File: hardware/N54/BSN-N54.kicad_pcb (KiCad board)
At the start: 4 copper layers, 34 x 34 mm, 44 parts, among them J1 Conn_Coaxial_Small, U1 nRF54L05-QFXX, U2 SHTC3, U3 HDC2010, X1 32MHz, X2 32.768kHz

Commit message: Cleaned up libraries for both variants
Renamed the project libraries to BSN-N54 / BSN-C23 and updated lib tables and all references, removed Nordic parts and the unused 40-pin CC2340 package from the C23 library, synced Antenna symbol fields to N54, updated READMEs.
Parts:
- AE1: footprint BLE_Sensor_Node:AANI-CH-0138-Q-T -> BSN-N54:AANI-CH-0138-Q-T
- U1: footprint BLE_Sensor_Node:VQFN-48-1EP_6x6mm_P0.4mm_EP4.1x4.1mm_ThermalVias -> BSN-N54:VQFN-48-1EP_6x6mm_P0.4mm_EP4.1x4.1mm_ThermalVias
- U3: footprint BLE_Sensor_Node:HDC2010 -> BSN-N54:HDC2010
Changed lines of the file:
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@@
 		)
 	)
-	(footprint "BLE_Sensor_Node:HDC2010"
+	(footprint "BSN-N54:HDC2010"
 		(layer "F.Cu")
 		(at 159.2 106 90)
@@
 		)
 	)
-	(footprint "BLE_Sensor_Node:VQFN-48-1EP_6x6mm_P0.4mm_EP4.1x4.1mm_ThermalVias"
+	(footprint "BSN-N54:VQFN-48-1EP_6x6mm_P0.4mm_EP4.1x4.1mm_ThermalVias"
 		(locked yes)
 		(layer "F.Cu")
@@
 		)
 		(embedded_fonts no)
-		(model "${KIPRJMOD}/library/3d_models/QFN-48-1EP_6x6_P04mm.STEP"
+		(model "${KIPRJMOD}/library/3d_models/VQFN-48-1EP_6x6mm_P0.4mm_EP4.1x4.1mm.step"
 			(offset
 				(xyz 0 0 0)
@@
 		)
 	)
-	(footprint "BLE_Sensor_Node:AANI-CH-0138-Q-T"
+	(footprint "BSN-N54:AANI-CH-0138-Q-T"
 		(layer "F.Cu")
 		(at 150 84.75)

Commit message: Slikscreen cleanup
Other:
- board text added: "INT"
- board text added: "SCL"
- board text added: "SDA"
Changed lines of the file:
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@@
 		)
 	)
-	(gr_text "RST"
+	(gr_text "SDA"
 		(at 160.1 103.4 0)
 		(layer "F.SilkS")
@@
 		)
 	)
-	(gr_text "RST"
+	(gr_text "SCL"
 		(at 160.8 100.8 0)
 		(layer "F.SilkS")
@@
 		)
 	)
-	(gr_text "RST"
+	(gr_text "INT"
 		(at 164.5 105.5 0)
 		(layer "F.SilkS")

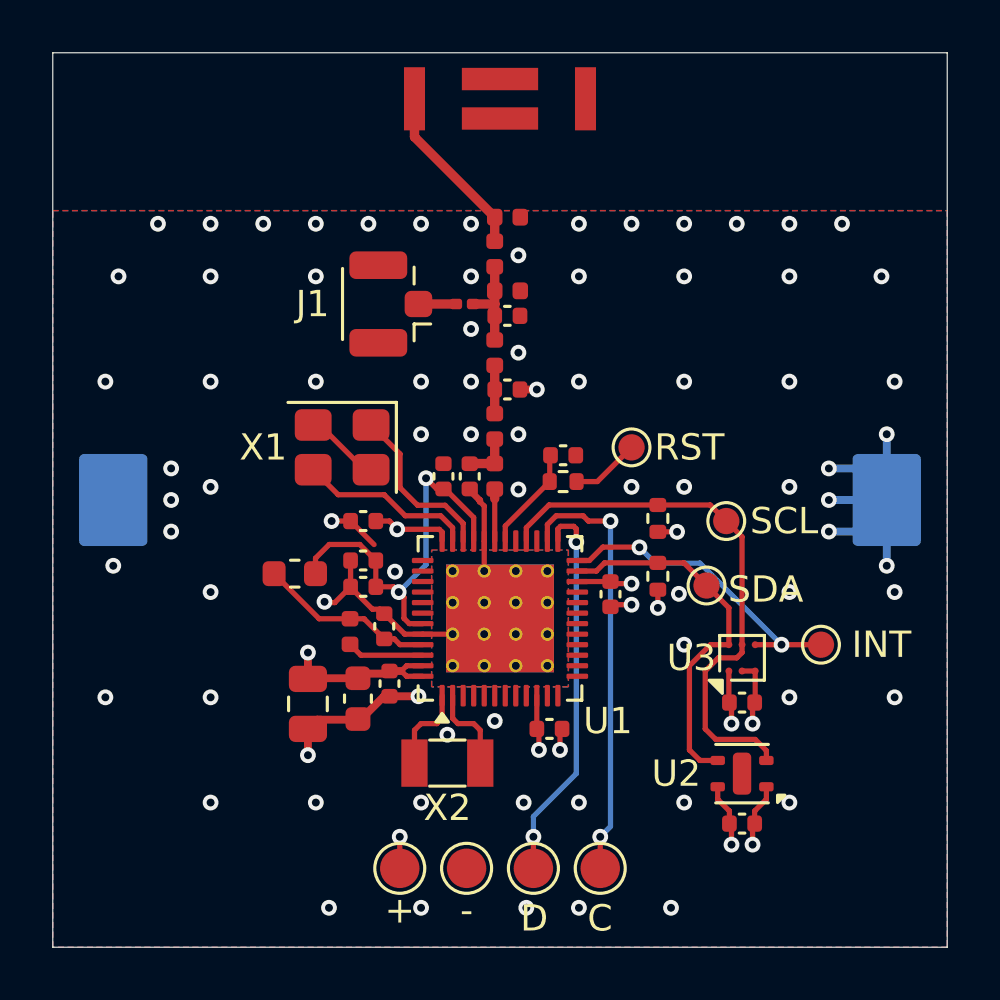
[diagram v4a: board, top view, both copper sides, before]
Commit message: Matched components & Footrpints. Small routing changes on N54
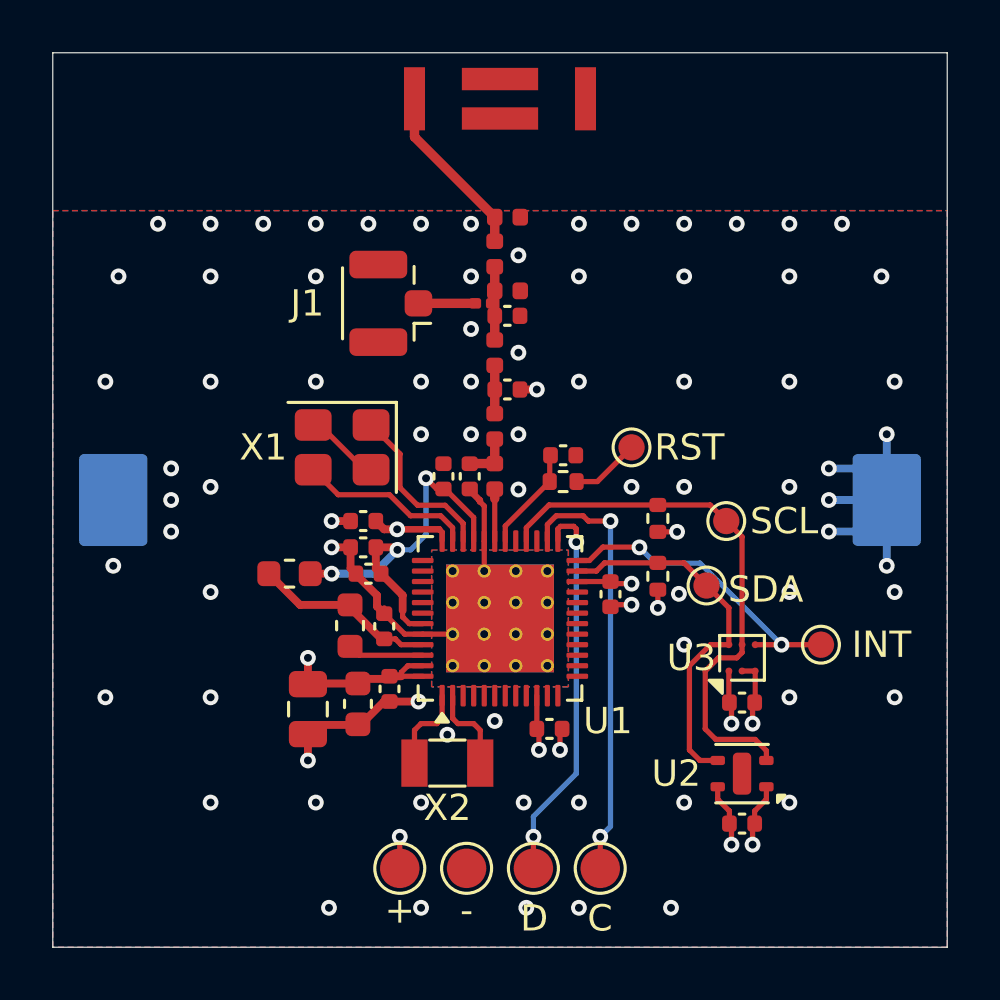
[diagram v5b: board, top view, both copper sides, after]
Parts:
- L1: footprint Inductor_SMD:L_0402_1005Metric -> Inductor_SMD:L_0603_1608Metric
- moved R4 0.73 mm to (149.4, 92.5)
- moved C7 0.54 mm to (145.0, 102.8)
- moved C8 0.50 mm to (144.8, 101.8)
- moved L1 0.22 mm to (144.3, 104.8)
- moved C1 0.20 mm to (144.6, 107.8)
- moved C10 0.20 mm to (142.7, 107.9)
- moved C2 0.20 mm to (145.8, 107.2)
- moved FB1 0.20 mm to (142.0, 102.8)
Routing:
- net GND: track 28.1 -> 26.9 mm, vias 78 -> 77
- net Net-(C16-Pad1): track 3.61 -> 2.78 mm
- net Net-(J1-In): track 1.43 -> 2.16 mm
- net Net-(U1-DECA): vias 2 -> 3

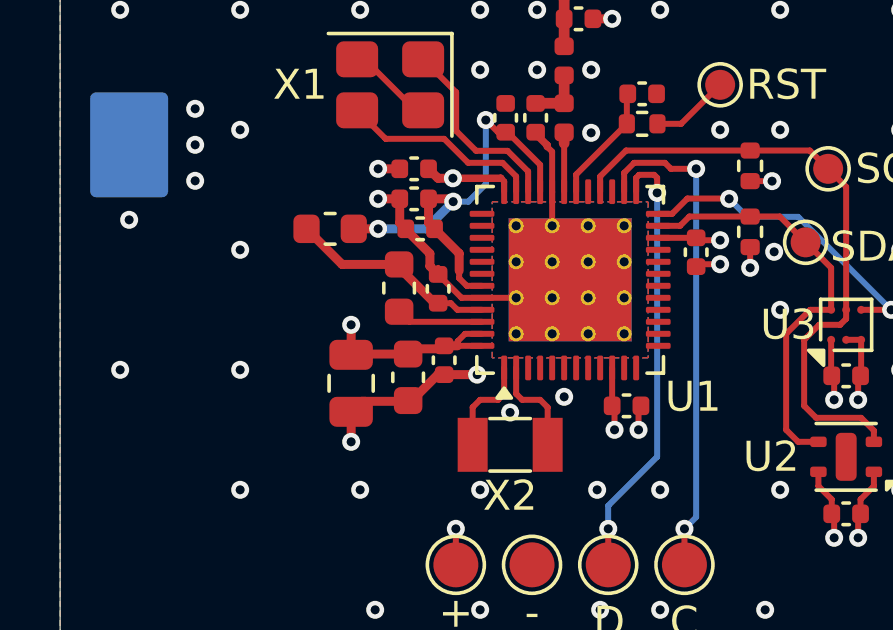
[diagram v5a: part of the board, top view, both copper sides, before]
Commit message: Progress on C23 layout & Routing
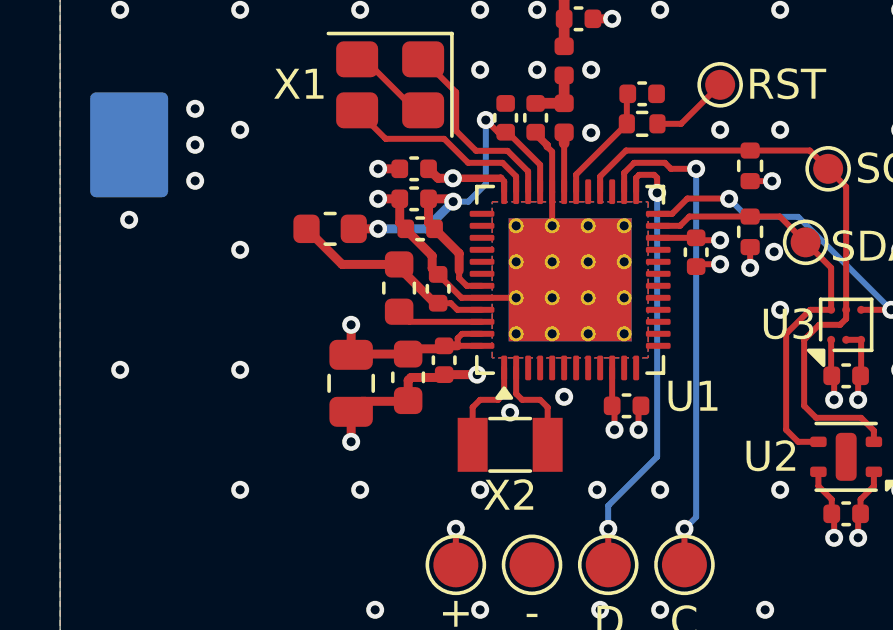
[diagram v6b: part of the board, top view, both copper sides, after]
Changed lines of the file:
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@@
-	)
-	(segment
-		(start 146.5 106.3)
-		(end 146.25 106.55)
-		(width 0.2)
-		(layer "F.Cu")
-		(net "VDD")
 	)
 	(segment
@@
 	)
 	(segment
+		(start 147.0625 106.3)
+		(end 146.4 106.3)
+		(width 0.2)
+		(layer "F.Cu")
+		(net "VDD")
+	)
+	(segment
 		(start 145.7 106.8)
 		(end 145.8 106.7)
@@
 	)
 	(segment
-		(start 147.0625 106.3)
-		(end 146.5 106.3)
-		(width 0.2)
-		(layer "F.Cu")
-		(net "VDD")
-	)
-	(segment
 		(start 144.6 106.975)
 		(end 144.775 106.8)
@@
 		(end 146.091302 101.114496)
 		(width 0.3)
+		(layer "F.Cu")
+		(net "VDD")
+	)
+	(segment
+		(start 146.25 106.45)
+		(end 146.25 106.7)
+		(width 0.2)
 		(layer "F.Cu")
 		(net "VDD")
@@
 	)
 	(segment
+		(start 146.4 106.3)
+		(end 146.25 106.45)
+		(width 0.2)
+		(layer "F.Cu")
+		(net "VDD")
+	)
+	(segment
 		(start 154.2 103.1)
 		(end 152.9375 103.1)
@@
 	)
 	(segment
-		(start 146.25 106.55)
-		(end 146.25 106.7)
-		(width 0.2)
-		(layer "F.Cu")
-		(net "VDD")
-	)
-	(segment
 		(start 142.725 106.975)
 		(end 142.7 107)
@@
 	)
 	(segment
+		(start 145.705 107.755)
+		(end 144.695 107.755)
+		(width 0.3)
+		(layer "F.Cu")
+		(net "GND")
+	)
+	(segment
 		(start 144.32 101.8)
 		(end 144.32 102.6)
@@
 	)
 	(segment
+		(start 144.52 102.82)
+		(end 145.4 103.7)
+		(width 0.3)
+		(layer "F.Cu")
+		(net "GND")
+	)
+	(segment
 		(start 159.2 106.499997)
 		(end 159.200002 106.499999)
@@
 		(start 144.575 108.55)
 		(end 143.049998 108.55)
+		(width 0.3)
+		(layer "F.Cu")
+		(net "GND")
+	)
+	(segment
+		(start 144.52 102.8)
+		(end 144.52 102.82)
 		(width 0.3)
 		(layer "F.Cu")
@@
 	)
 	(segment
-		(start 145.59 107.66)
-		(end 144.725 108.525)
-		(width 0.3)
-		(layer "F.Cu")
-		(net "GND")
-	)
-	(segment
 		(start 159.7 107.679999)
 		(end 159.68 107.699999)
@@
 	)
 	(segment
-		(start 144.725 108.525)
-		(end 144.6 108.525)
-		(width 0.3)
-		(layer "F.Cu")
-		(net "GND")
-	)
-	(segment
 		(start 159.7 106.5)
 		(end 159.7 107.679999)
@@
 	(segment
 		(start 145.8 107.66)
-		(end 145.59 107.66)
+		(end 145.705 107.755)
 		(width 0.3)
 		(layer "F.Cu")
@@
 	)
 	(segment
-		(start 145.324926 104.044926)
-		(end 145.6 104.32)
-		(width 0.3)
-		(layer "F.Cu")
-		(net "GND")
-	)
-	(segment
-		(start 145.6 104.32)
-		(end 145.6 104.1)
-		(width 0.2)
-		(layer "F.Cu")
-		(net "GND")
-	)
-	(segment
 		(start 154.280001 103.98)
 		(end 154.200001 104.06)
@@
 	)
 	(segment
-		(start 144.52 102.8)
-		(end 144.52 102.82)
+		(start 144.695 107.755)
+		(end 144.6 107.85)
 		(width 0.3)
 		(layer "F.Cu")
@@
 		(end 152.36 108.7)
 		(width 0.2)
+		(layer "F.Cu")
+		(net "GND")
+	)
+	(segment
+		(start 145.4 104.12)
+		(end 145.6 104.32)
+		(width 0.3)
 		(layer "F.Cu")
 		(net "GND")
@@
 	)
 	(segment
-		(start 145.324926 103.624926)
-		(end 145.324926 104.044926)
-		(width 0.3)
-		(layer "F.Cu")
-		(net "GND")
-	)
-	(segment
 		(start 144.32 102.6)
 		(end 144.52 102.8)
@@
 	)
 	(segment
-		(start 144.52 102.82)
-		(end 145.324926 103.624926)
-		(width 0.3)
-		(layer "F.Cu")
-		(net "GND")
-	)
-	(segment
 		(start 149.4 101.5625)
 		(end 149.4 102.7)
@@
 	)
 	(segment
+		(start 145.4 103.7)
+		(end 145.4 104.12)
+		(width 0.3)
+		(layer "F.Cu")
+		(net "GND")
+	)
+	(segment
 		(start 144.85 98.85)
 		(end 143.15 97.15)
@@
 		(end 159.6 107.78)
 		(width 0.2)
+		(layer "F.Cu")
+		(net "GND")
+	)
+	(segment
+		(start 144.6 107.85)
+		(end 144.6 108.525)
+		(width 0.3)
 		(layer "F.Cu")
 		(net "GND")
@@
 			)
 		)
+	)
+	(zone
+		(layer "F.Cu")
+		(hatch edge 0.5)
+		(connect_pads
+			(clearance 0)
+		)
+		(min_thickness 0.15)
+		(keepout
+			(tracks allowed)
+			(vias allowed)
+			(pads allowed)
+			(copperpour not_allowed)
+			(footprints allowed)
+		)
+		(placement
+			(enabled no)
+			(sheetname "/")
+		)
+		(fill
+			(thermal_gap 0.5)
+			(thermal_bridge_width 0.3)
+			(island_removal_mode 0)
+		)
+		(polygon
+			(pts
+				(xy 143.25 97.4) (xy 144.75 97.4) (xy 144.75 98.2) (xy 144.25 98.7) (xy 143.75 98.7) (xy 143.25 98.2)
+			)
+		)
+	)
+	(zone
+		(layer "F.Cu")
+		(hatch edge 0.5)
+		(connect_pads
+			(clearance 0)
+		)
+		(min_thickness 0.15)
+		(keepout
+			(tracks allowed)
+			(vias allowed)
+			(pads allowed)
+			(copperpour not_allowed)
+			(footprints allowed)
+		)
+		(placement
+			(enabled no)
+			(sheetname "/")
+		)
+		(fill
+			(thermal_gap 0.5)
+			(thermal_bridge_width 0.3)
+			(island_removal_mode 0)
+		)
+		(polygon
+			(pts
+				(xy 144.65 103.15) (xy 146.15 103.15) (xy 146.15 103.95) (xy 145.65 104.45) (xy 145.15 104.45) (xy 144.65 103.95)
+			)
+		)
+	)
+	(zone
+		(layer "F.Cu")
+		(hatch edge 0.5)
+		(connect_pads
+			(clearance 0)
+		)
+		(min_thickness 0.15)
+		(keepout
+			(tracks allowed)
+			(vias allowed)
+			(pads allowed)
+			(copperpour not_allowed)
+			(footprints allowed)
+		)
+		(placement
+			(enabled no)
+			(sheetname "/")
+		)
+		(fill
+			(thermal_gap 0.5)
+			(thermal_bridge_width 0.3)
+			(island_removal_mode 0)
+		)
+		(polygon
+			(pts
+				(xy 142.85 106.75) (xy 144.386434 106.75) (xy 144.386434 107.55) (xy 143.886434 108.05) (xy 142.85 108.05)
+			)
+		)

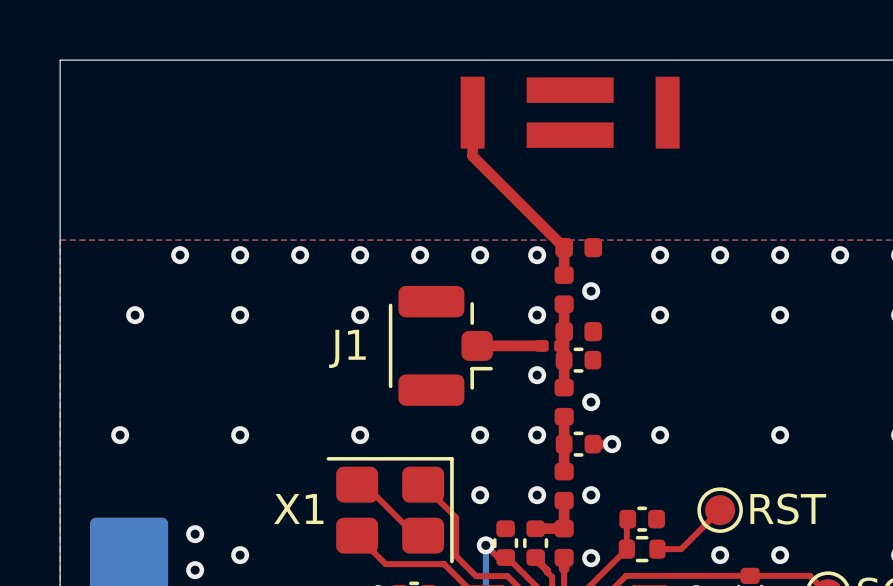
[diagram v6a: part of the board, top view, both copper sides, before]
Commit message: Moved the U.FL connector closer to the matching network
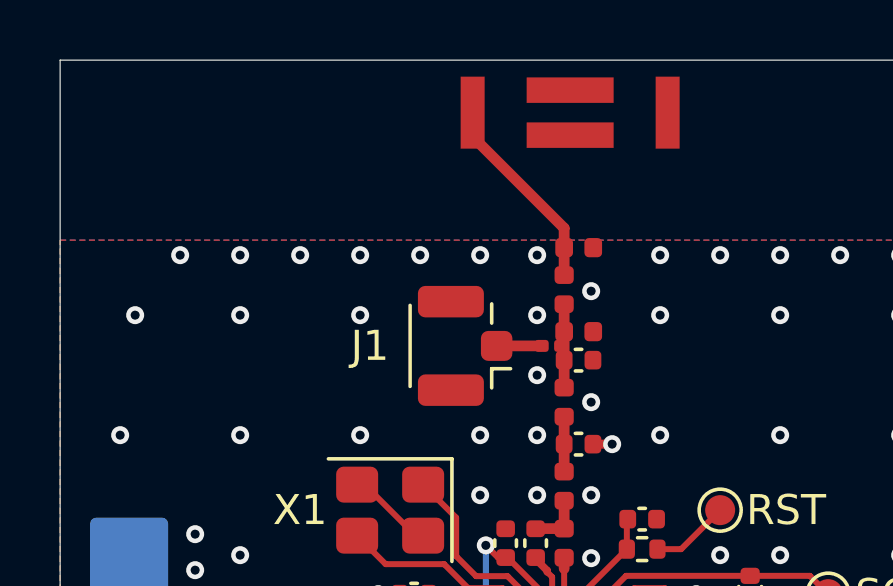
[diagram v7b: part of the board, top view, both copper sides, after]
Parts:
- moved J1 0.65 mm to (146.0, 92.5)
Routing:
- net Net-(J1-In): track 2.16 -> 1.50 mm
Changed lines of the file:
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@@
 	(footprint "Connector_Coaxial:U.FL_Hirose_U.FL-R-SMT-1_Vertical"
 		(layer "F.Cu")
-		(at 145.375 92.525 180)
+		(at 146.025 92.525 180)
 		(descr "Hirose U.FL Coaxial (https://www.hirose.com/en/product/document?clcode=CL0331-0472-2-01&productname=U.FL-R-SMT-1(01)&series=U.FL&documenttype=2DDrawing&lang=en&documentid=0000940668)")
 		(tags "Hirose U.FL Coaxial")
@@
 			(polygon
 				(pts
-					(xy 144.275 93.475) (xy 146.365 93.475) (xy 146.365 91.575) (xy 144.275 91.575)
+					(xy 144.925 93.475) (xy 147.015 93.475) (xy 147.015 91.575) (xy 144.925 91.575)
 				)
 			)
@@
 	)
 	(segment
-		(start 149.8 89.25)
-		(end 146.75 86.2)
+		(start 149.8 90.165)
+		(end 149.8 89.25)
 		(width 0.3586)
 		(layer "F.Cu")
@@
 	)
 	(segment
-		(start 149.8 90.165)
-		(end 149.8 89.25)
+		(start 149.8 89.25)
+		(end 149.8 88.6)
 		(width 0.3586)
 		(layer "F.Cu")
@@
 	)
 	(segment
-		(start 146.75 86.2)
+		(start 146.75 85.55)
 		(end 146.75 84.75)
 		(width 0.3586)
@@
 	)
 	(segment
+		(start 149.8 88.6)
+		(end 146.75 85.55)
+		(width 0.3586)
+		(layer "F.Cu")
+		(net "/ANT")
+	)
+	(segment
 		(start 155.3 101.8)
 		(end 155.290001 101.790001)
@@
 	)
 	(segment
-		(start 146.9 92.525)
+		(start 147.55 92.525)
 		(end 149.055 92.525)
 		(width 0.3586)
@@
 		(polygon
 			(pts
-				(xy 149.2 100.7) (xy 149.2 88.9) (xy 150.4 88.9) (xy 150.4 100.7)
-			)
-		)
-	)
-	(zone
-		(layer "F.Cu")
-		(hatch edge 0.5)
-		(connect_pads
-			(clearance 0)
-		)
-		(min_thickness 0.2)
-		(keepout
-			(tracks allowed)
-			(vias allowed)
-			(pads allowed)
-			(copperpour not_allowed)
-			(footprints allowed)
-		)
-		(placement
-			(enabled no)
-			(sheetname "/")
-		)
-		(fill
-			(thermal_gap 0.5)
-			(thermal_bridge_width 0.3)
-			(island_removal_mode 0)
-		)
-		(polygon
-			(pts
 				(xy 152.4 102.1) (xy 152.4 106.9) (xy 147.6 106.9) (xy 147.6 102.1) (xy 152.2 102.1) (xy 152.2 102.3)
 				(xy 147.8 102.3) (xy 147.8 106.7) (xy 152.2 106.7) (xy 152.2 102.1)
@@
 			)
 		)
+	)
+	(zone
+		(layers "F.Cu" "In1.Cu" "In2.Cu")
+		(hatch edge 0.5)
+		(connect_pads
+			(clearance 0)
+		)
+		(min_thickness 0.2)
+		(keepout
+			(tracks allowed)
+			(vias allowed)
+			(pads allowed)
+			(copperpour not_allowed)
+			(footprints allowed)
+		)
+		(placement
+			(enabled no)
+			(sheetname "/")
+		)
+		(fill
+			(thermal_gap 0.5)
+			(thermal_bridge_width 0.3)
+			(island_removal_mode 0)
+		)
+		(polygon
+			(pts
+				(xy 149.2 100.7) (xy 149.2 88.9) (xy 150.4 88.9) (xy 150.4 100.7)
+			)
+		)
